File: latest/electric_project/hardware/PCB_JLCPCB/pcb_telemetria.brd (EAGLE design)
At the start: 106.8 x 120.2 mm, 43 parts

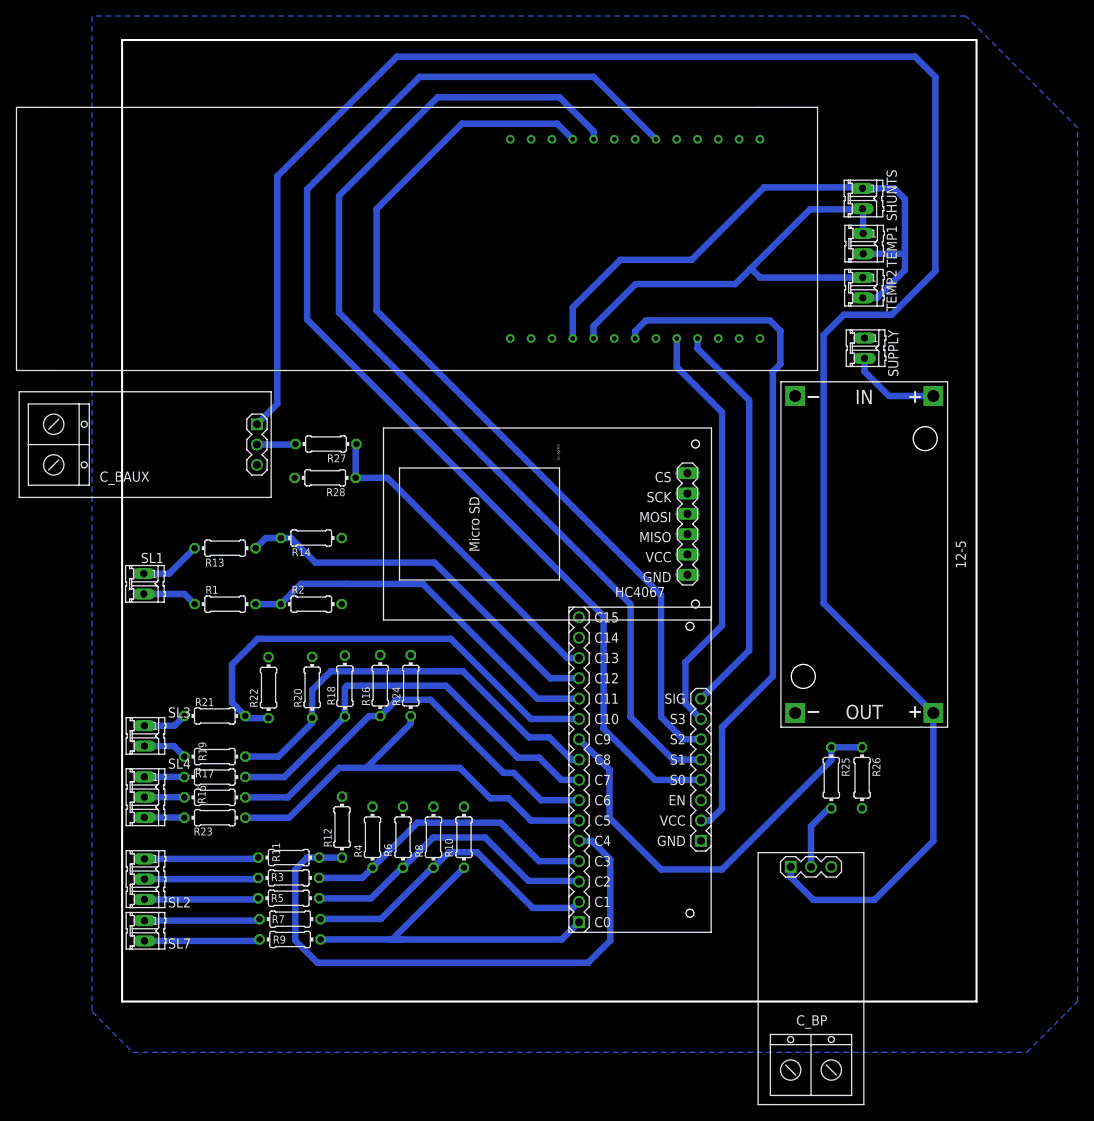
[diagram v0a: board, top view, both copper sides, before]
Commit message: placa com trilhas finas e Mini-fit molex
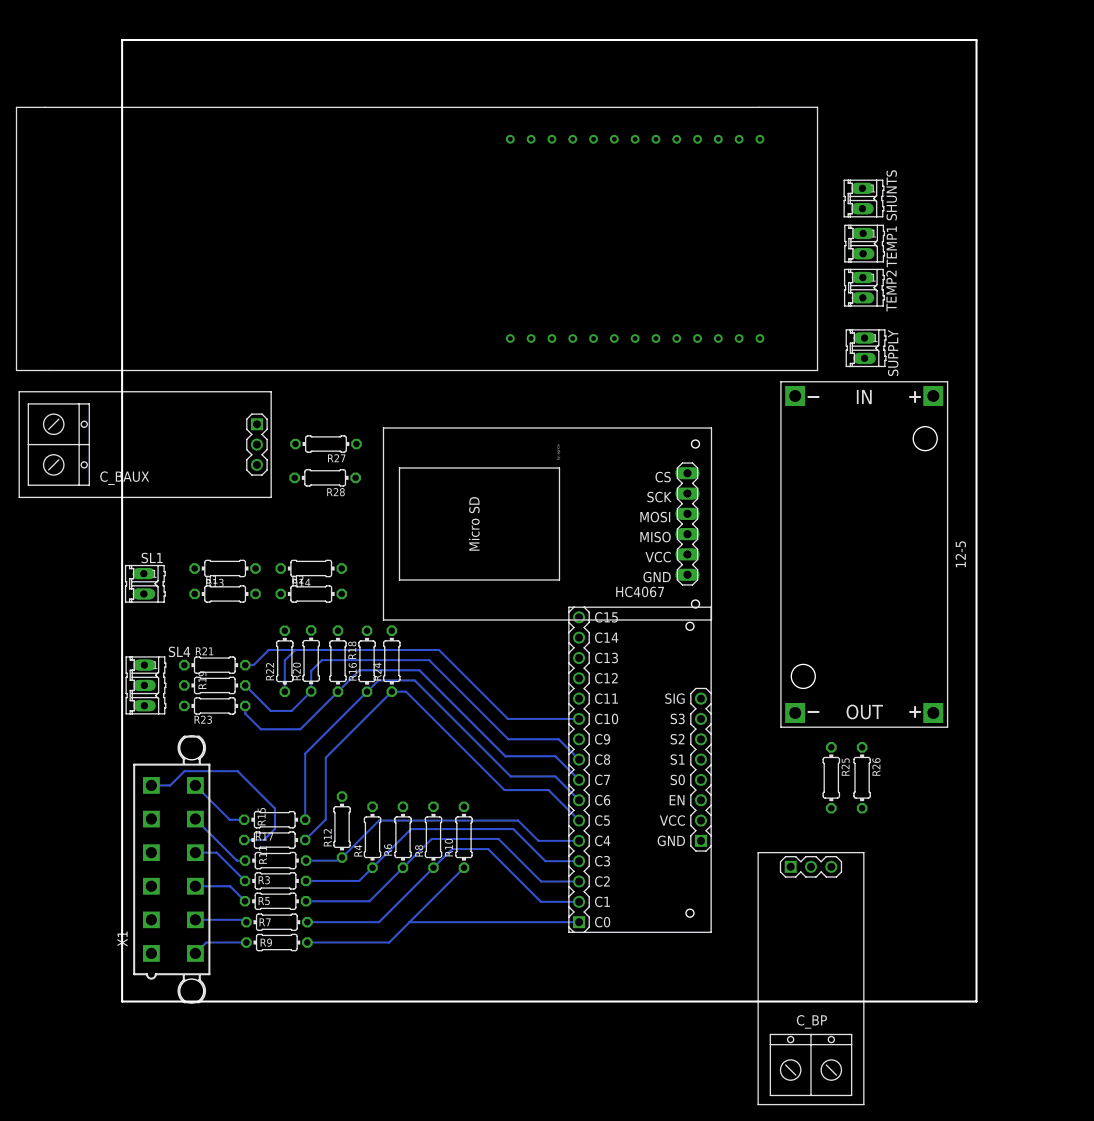
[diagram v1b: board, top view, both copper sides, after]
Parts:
- removed SL2: (no value), con-amp-quick:03P
- removed SL3, SL7: (no value), con-amp-quick:02P
- added X1: 5566-12, con-molex:5566-12
- moved SL4 14.0 mm to (6.54, 35.7)
- moved R23 14.0 mm to (15.3, 33.1)
- moved R17 10.9 mm to (22.8, 16.4)
- moved R19 8.89 mm to (15.3, 35.7)
- moved R15 8.00 mm to (22.8, 18.9)
- moved R21 6.35 mm to (15.3, 38.2)
- moved R22 3.88 mm to (24.1, 38.7)
- moved R24 3.86 mm to (37.5, 38.7)
- moved R14 3.81 mm to (27.4, 50.3)
- moved R16 3.47 mm to (34.4, 38.7)
- moved R20 3.30 mm to (27.4, 38.8)
- moved R18 3.23 mm to (30.7, 38.7)
- moved R13 2.54 mm to (16.6, 50.3)
- moved R11 1.69 mm to (22.9, 13.8)
- moved R5 1.69 mm to (22.9, 8.72)
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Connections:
- new net GND3: R24.2
- new net N$5: X1.2
- new net N$6: X1.1
- new net N$8: X1.5
- net 21: now also X1.4
- net 22: now also X1.3
- net BAT_AUX: now also SL4.1; no longer SL3.1
- net BB_IN: now also X1.12; no longer SL4.2
- net BE_IN: now also X1.6; no longer SL4.1
- net BTN_CRUZ: now also X1.10; no longer SL2.2
- net BTN_M: now also X1.9; no longer SL2.3
- net BTN_RE: now also X1.8; no longer SL7.1
- net C5: now also R17.1; no longer R23.2
- net C7: now also R23.2; no longer R17.1
- net COOLER_E: now also SL4.2; no longer SL3.2
- net DMS_IN: now also X1.7; no longer SL7.2
- net GND: no longer R24.2
- net POT_IN: now also X1.11; no longer SL2.1
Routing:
- net VCC: track 255.4 -> 0.00 mm
- net 32: track 150.3 -> 0.00 mm
- net 14: track 130.9 -> 0.00 mm
- net 13: track 114.1 -> 0.00 mm
- net 3V3: track 86.1 -> 0.00 mm
- net 21: track 73.0 -> 0.00 mm
- net 22: track 58.9 -> 0.00 mm
- net C9: track 52.9 -> 0.00 mm
- net 0: track 52.6 -> 0.00 mm
- net 4: track 50.2 -> 0.00 mm
- net C12: track 48.2 -> 0.00 mm
- net C11: track 47.4 -> 0.00 mm
- net C13: track 41.5 -> 0.00 mm
- net C4: track 72.0 -> 37.3 mm
- net BE_IN: track 5.00 -> 25.1 mm
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- removed copper zone on layer 16, net GND

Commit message: update
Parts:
- moved U$2 4.58 mm to (77.0, 59.7)
- moved R25 3.81 mm to (88.6, 24.2)
- moved R26 3.81 mm to (92.4, 24.2)
- moved X1 1.27 mm to (10.2, 14.0)
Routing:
- net POT_IN: track 8.36 -> 9.78 mm
- net BB_IN: track 7.89 -> 8.83 mm
- net DMS_IN: track 6.94 -> 6.41 mm
- net BTN_M: track 6.99 -> 7.51 mm
- net BTN_CRUZ: track 7.67 -> 8.20 mm
- net BTN_RE: track 6.50 -> 7.02 mm
- net BE_IN: track 25.1 -> 25.6 mm
